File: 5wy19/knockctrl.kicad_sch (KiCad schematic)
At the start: 3 parts, among them IC5 TP1C8101DW

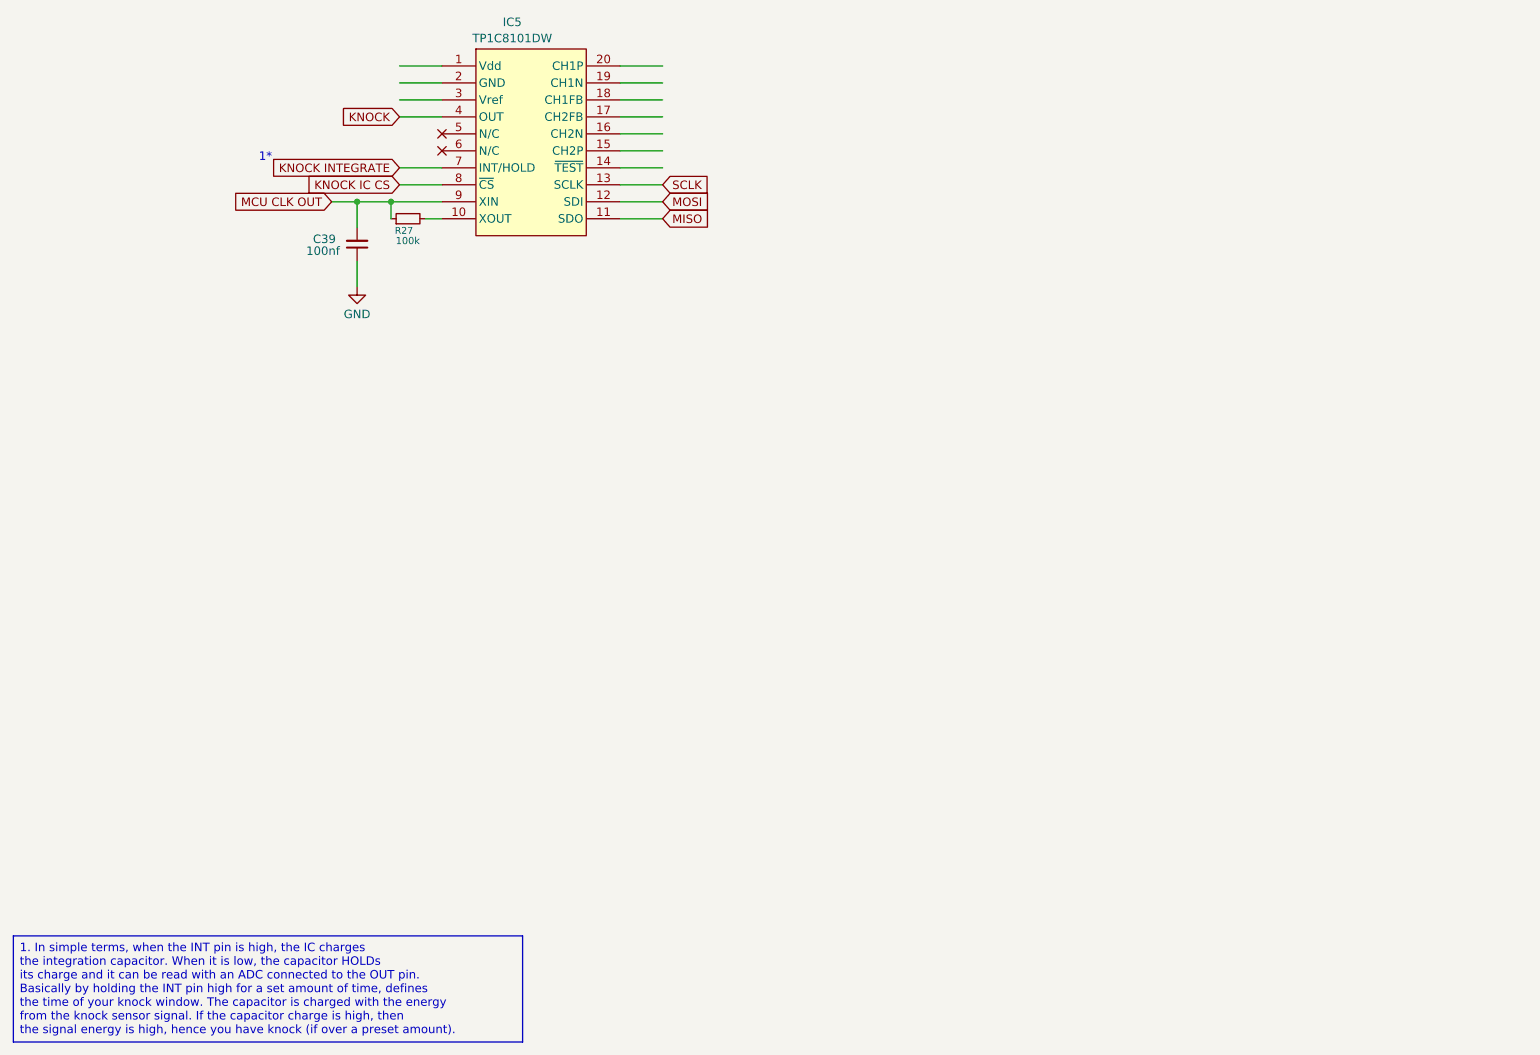
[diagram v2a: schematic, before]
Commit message: Finished most of the subsystems
-- MCU finished
-- Flash finished
-- Power Supply finished
-- I/O Drivers finished
-- CANBUS finished
-- Knock Control finished
-- Connector finished
-- Ignition Driver finished
-- Sensor Logic mostly finished
-- Logic ICs need some work
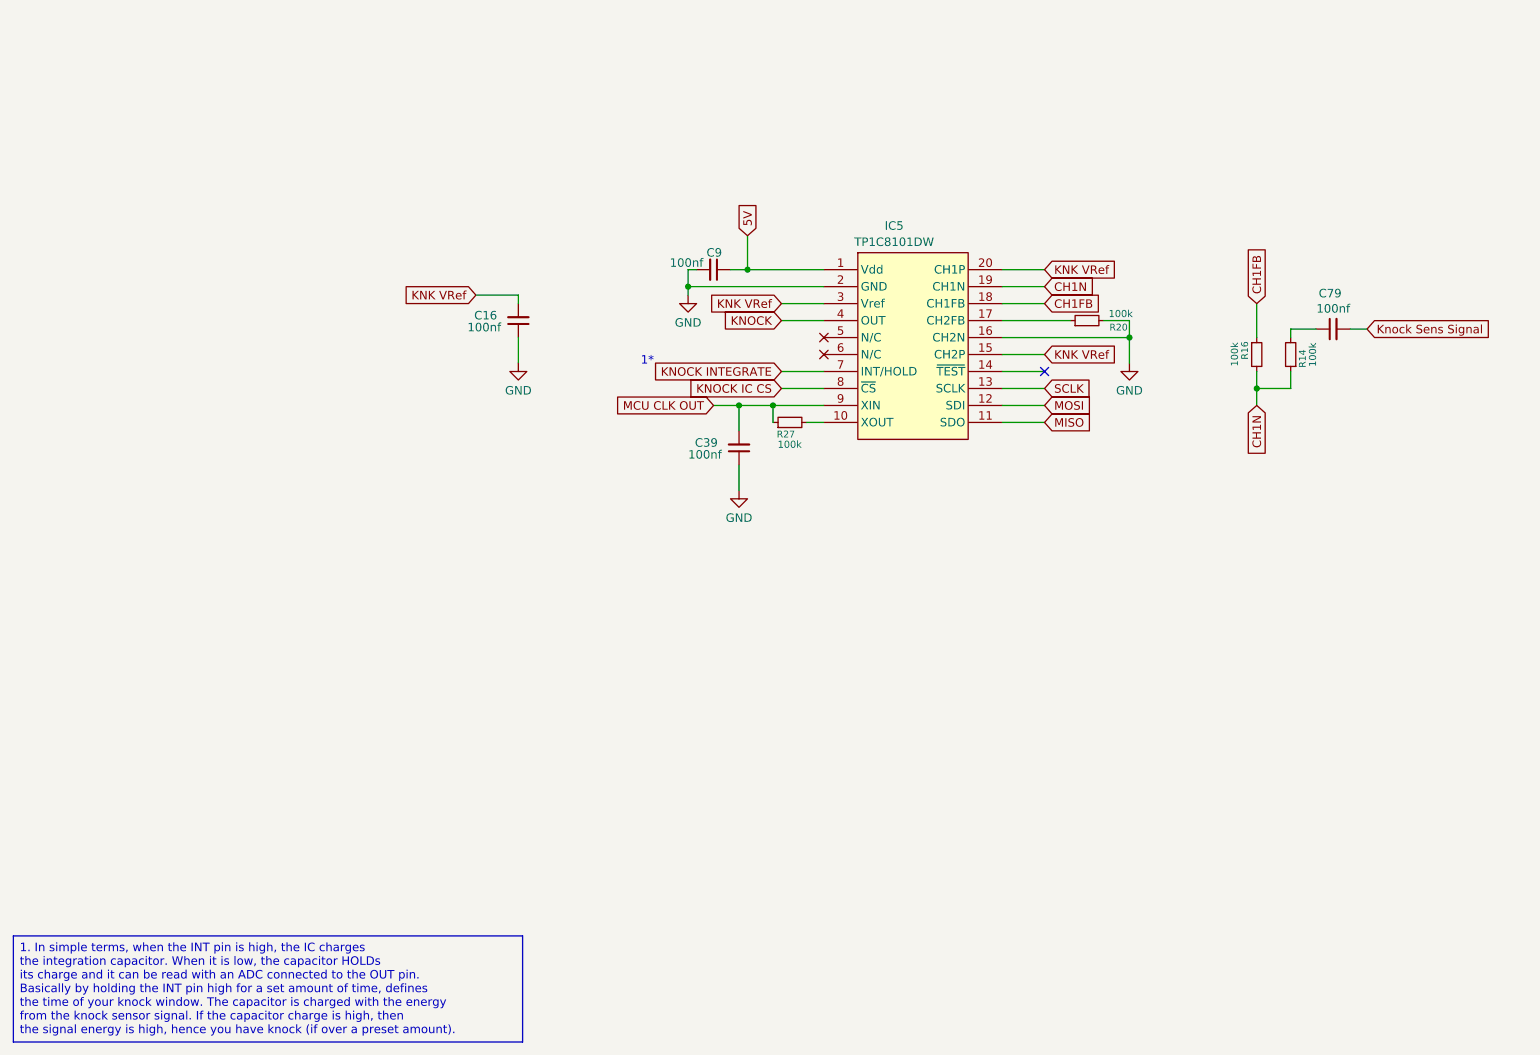
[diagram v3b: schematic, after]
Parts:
- added C16, C79, C9: 100nf, symbol Device:C_Small
- added R14, R16, R20: 100k, symbol Device:R_Small
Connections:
- net GND: now also IC5.16 (CH2N), IC5.2 (GND), C16.1, C9.2, R20.2
- net 5V: now reaches IC5.1 (Vdd)
- net 5V: now also C9.1
- net KNK VRef: now reaches IC5.15 (CH2P)
- net KNK VRef: now also IC5.20 (CH1P), IC5.3 (Vref), C16.2
- net at IC5.17 (CH2FB): now also R20.1
- net CH1FB: now reaches IC5.18 (CH1FB)
- net CH1FB: now also R16.1
- net CH1N: now reaches IC5.19 (CH1N)
- net CH1N: now also R14.1, R16.2
- new net: C79.1, R14.2
- new net Knock Sens Signal: C79.2
- no-connect marks 0 -> 1
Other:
- title: (none) -> SMIK43 5WY19 Rev. Eng
- moved on the sheet: C39, IC5, R27

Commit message: Final schematic (except maybe some oversights)
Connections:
- net CH1N: now also R14.2; no longer R14.1
- net GND: now also C16.2; no longer C16.1
- net KNK VRef: now also C16.1; no longer C16.2
- net at C79.1: now also R14.1; no longer R14.2
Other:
- moved on the sheet: C16, R14
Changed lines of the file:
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@@
 	(symbol
 		(lib_id "Device:C_Small")
-		(at 87.63 90.17 180)
+		(at 87.63 90.17 0)
 		(unit 1)
 		(exclude_from_sim no)
@@
 		(dnp no)
 		(property "Reference" "C16"
-			(at 81.026 89.408 0)
+			(at 94.234 90.932 0)
 			(effects
 				(font
@@
 		)
 		(property "Value" "100nf"
-			(at 80.01 91.186 0)
+			(at 95.25 89.154 0)
 			(effects
 				(font
@@
 	(symbol
 		(lib_id "Device:R_Small")
-		(at 203.2 95.25 180)
+		(at 203.2 95.25 0)
 		(unit 1)
 		(exclude_from_sim no)
@@
 		(dnp no)
 		(property "Reference" "R14"
-			(at 204.978 94.488 90)
+			(at 201.422 96.012 90)
 			(effects
 				(font
@@
 		)
 		(property "Value" "100k"
-			(at 206.502 93.472 90)
-			(effects
-				(font
+			(at 199.898 97.028 90)
+			(effects
+				(font
